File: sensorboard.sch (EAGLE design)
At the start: 18 parts, among them U1 LM1117MP-3.3, U2 LM324D

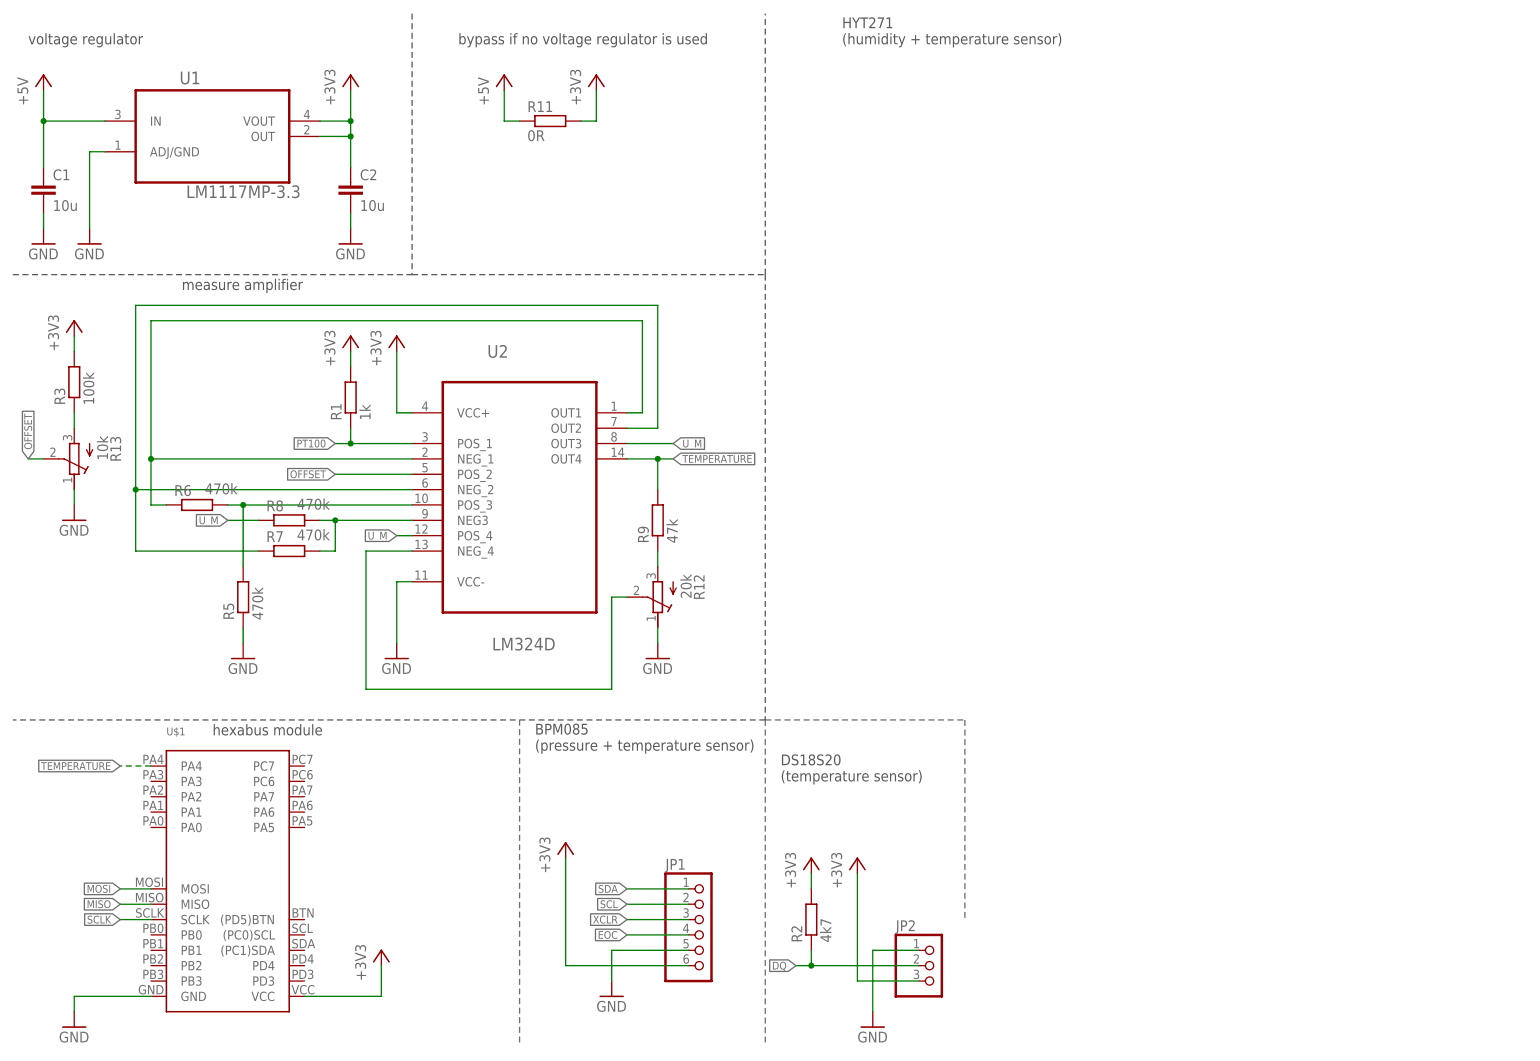
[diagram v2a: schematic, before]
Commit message: added HYT271
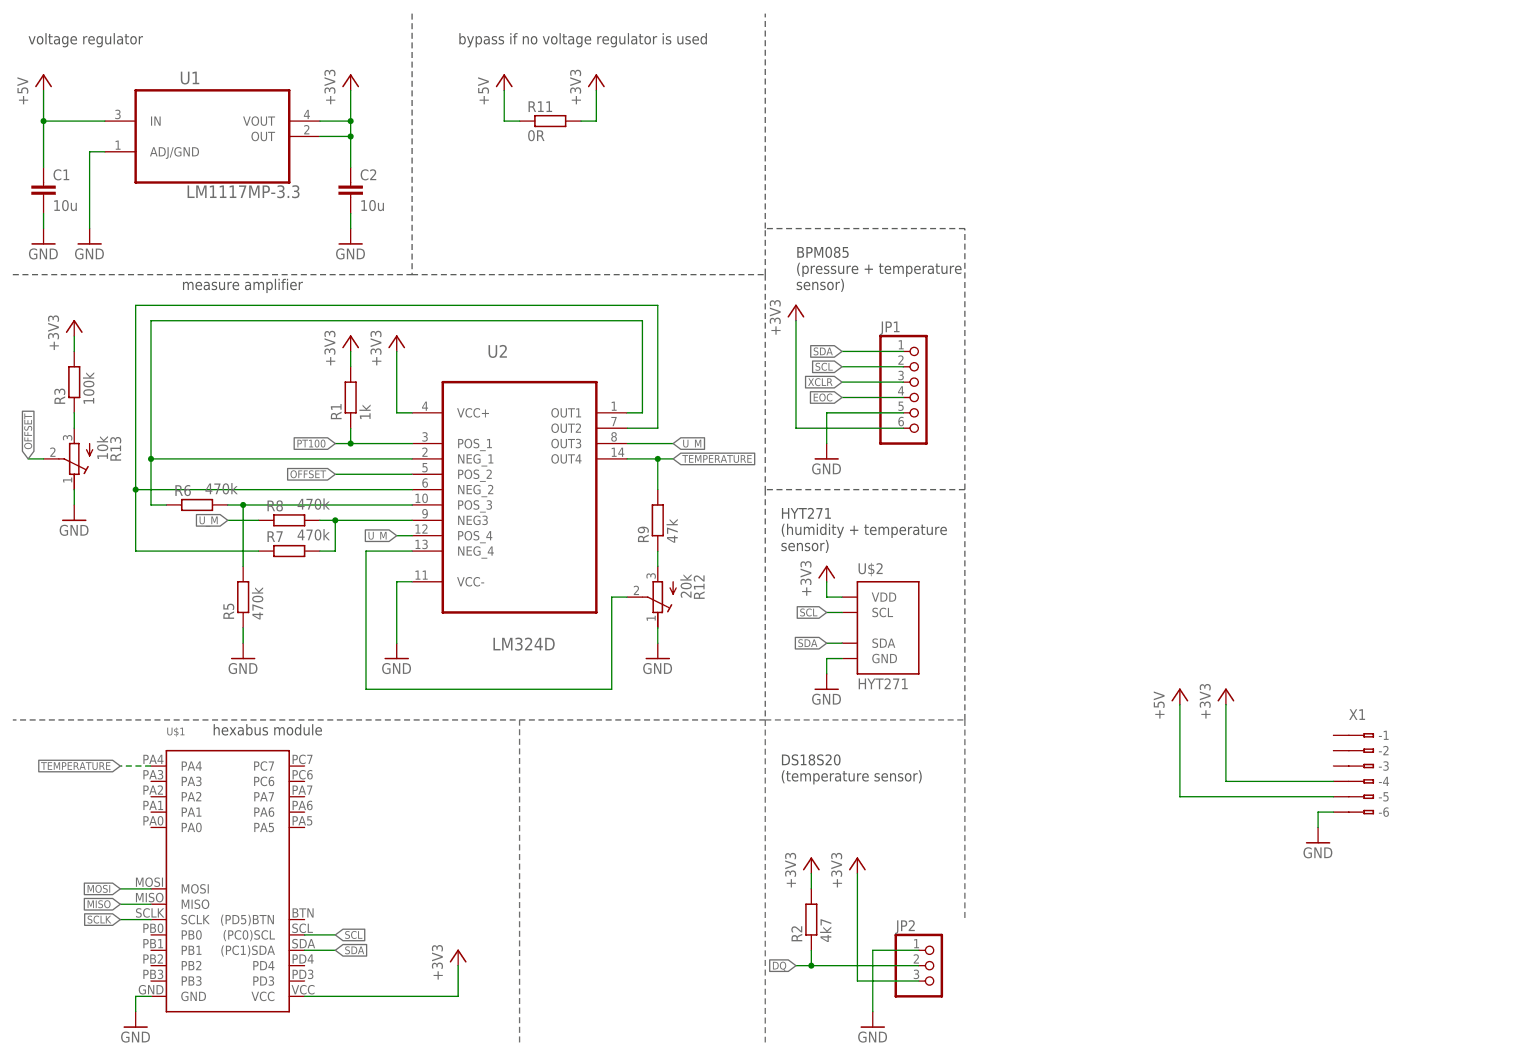
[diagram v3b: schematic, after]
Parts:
- added U$2: HYT271, humidity:HYT271
- added X1: (no value), con-wago:233-206
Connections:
- net +3V3: now also U$2.VDD, X1.B-4
- net +5V: now also X1.B-5
- net GND: now also U$2.GND, X1.B-6
- net SCL: now also U$1.(PC0)SCL, U$2.SCL
- net SDA: now also U$1.(PC1)SDA, U$2.SDA
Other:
- moved on the sheet: JP1

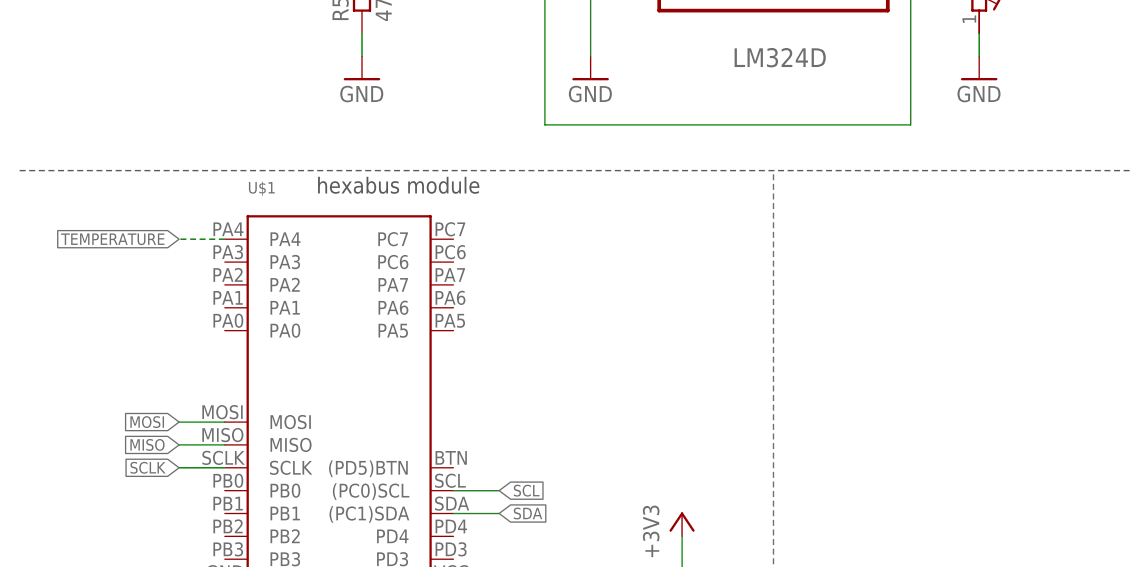
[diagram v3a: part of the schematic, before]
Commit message: connector for SPI, I2C and onewire
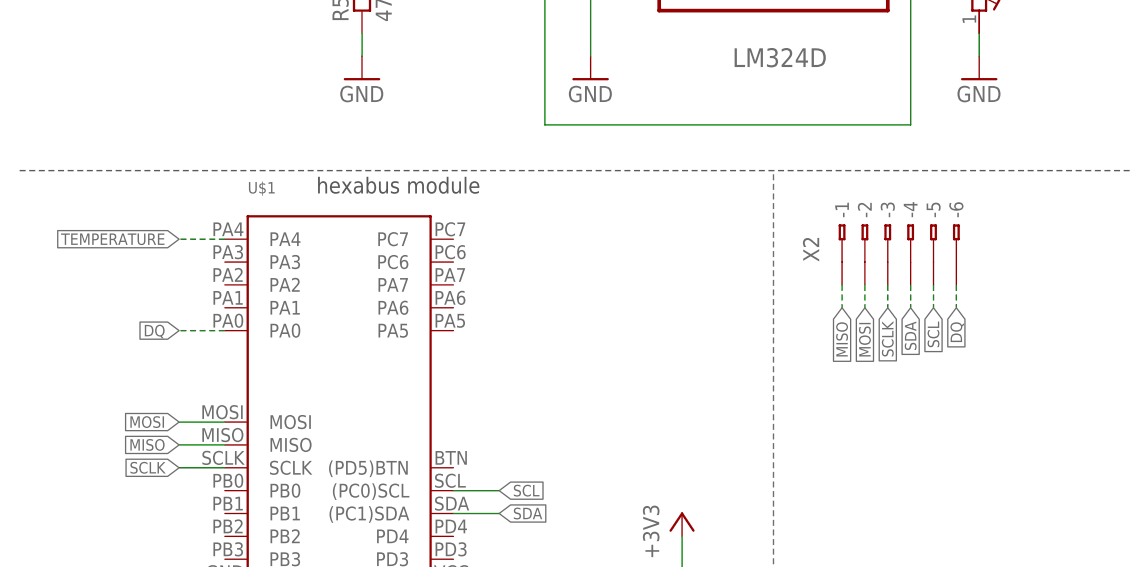
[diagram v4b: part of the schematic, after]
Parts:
- added X2: (no value), con-wago:233-206
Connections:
- net DQ: now also U$1.PA0, X2.B-6
- net MISO: now also X2.B-1
- net MOSI: now also X2.B-2
- net SCL: now also X2.B-5
- net SCLK: now also X2.B-3
- net SDA: now also X2.B-4
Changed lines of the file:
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@@
 <part name="+3V11" library="supply1" deviceset="+3V3" device=""/>
 <part name="GND12" library="supply1" deviceset="GND" device=""/>
+<part name="X2" library="con-wago" deviceset="233-206" device=""/>
 </parts>
 <sheets>
@@
 <instance part="+3V11" gate="G$1" x="139.7" y="83.82"/>
 <instance part="GND12" gate="1" x="139.7" y="63.5"/>
+<instance part="X2" gate="G$1" x="101.6" y="53.34" rot="R90"/>
 </instances>
 <busses>
@@
 <label x="22.86" y="30.48" size="1.27" layer="95" rot="R180" xref="yes"/>
 </segment>
+<segment>
+<pinref part="X2" gate="G$1" pin="B-2"/>
+<wire x1="99.06" y1="45.72" x2="99.06" y2="43.18" width="0.1524" layer="91" style="longdash"/>
+<label x="99.06" y="43.18" size="1.27" layer="95" rot="R270" xref="yes"/>
+</segment>
 </net>
 <net name="MISO" class="0">
@@
 <label x="22.86" y="27.94" size="1.27" layer="95" rot="R180" xref="yes"/>
 </segment>
+<segment>
+<pinref part="X2" gate="G$1" pin="B-1"/>
+<wire x1="96.52" y1="45.72" x2="96.52" y2="43.18" width="0.1524" layer="91" style="longdash"/>
+<label x="96.52" y="43.18" size="1.27" layer="95" rot="R270" xref="yes"/>
+</segment>
 </net>
 <net name="SCLK" class="0">
@@
 <label x="22.86" y="25.4" size="1.27" layer="95" rot="R180" xref="yes"/>
 </segment>
+<segment>
+<pinref part="X2" gate="G$1" pin="B-3"/>
+<wire x1="101.6" y1="45.72" x2="101.6" y2="43.18" width="0.1524" layer="91" style="longdash"/>
+<label x="101.6" y="43.18" size="1.27" layer="95" rot="R270" xref="yes"/>
+</segment>
 </net>
 <net name="SDA" class="0">
@@
 <label x="58.42" y="20.32" size="1.27" layer="95" xref="yes"/>
 </segment>
+<segment>
+<pinref part="X2" gate="G$1" pin="B-4"/>
+<wire x1="104.14" y1="45.72" x2="104.14" y2="43.18" width="0.1524" layer="91" style="longdash"/>
+<label x="104.14" y="43.18" size="1.27" layer="95" rot="R270" xref="yes"/>
+</segment>
 </net>
 <net name="SCL" class="0">
@@
 <wire x1="53.34" y1="22.86" x2="58.42" y2="22.86" width="0.1524" layer="91"/>
 <label x="58.42" y="22.86" size="1.27" layer="95" xref="yes"/>
+</segment>
+<segment>
+<pinref part="X2" gate="G$1" pin="B-5"/>
+<wire x1="106.68" y1="45.72" x2="106.68" y2="43.18" width="0.1524" layer="91" style="longdash"/>
+<label x="106.68" y="43.18" size="1.27" layer="95" rot="R270" xref="yes"/>
 </segment>
 </net>
@@
 <label x="134.62" y="17.78" size="1.27" layer="95" rot="R180" xref="yes"/>
 </segment>
-</net>
+<segment>
+<pinref part="U$1" gate="G$1" pin="PA0"/>
+<wire x1="27.94" y1="40.64" x2="22.86" y2="40.64" width="0.1524" layer="91" style="longdash"/>
+<label x="22.86" y="40.64" size="1.27" layer="95" rot="R180" xref="yes"/>
+</segment>
+<segment>
+<pinref part="X2" gate="G$1" pin="B-6"/>
+<wire x1="109.22" y1="45.72" x2="109.22" y2="43.18" width="0.1524" layer="91" style="longdash"/>
+<label x="109.22" y="43.18" size="1.27" layer="95" rot="R270" xref="yes"/>
+</segment>
+</net>

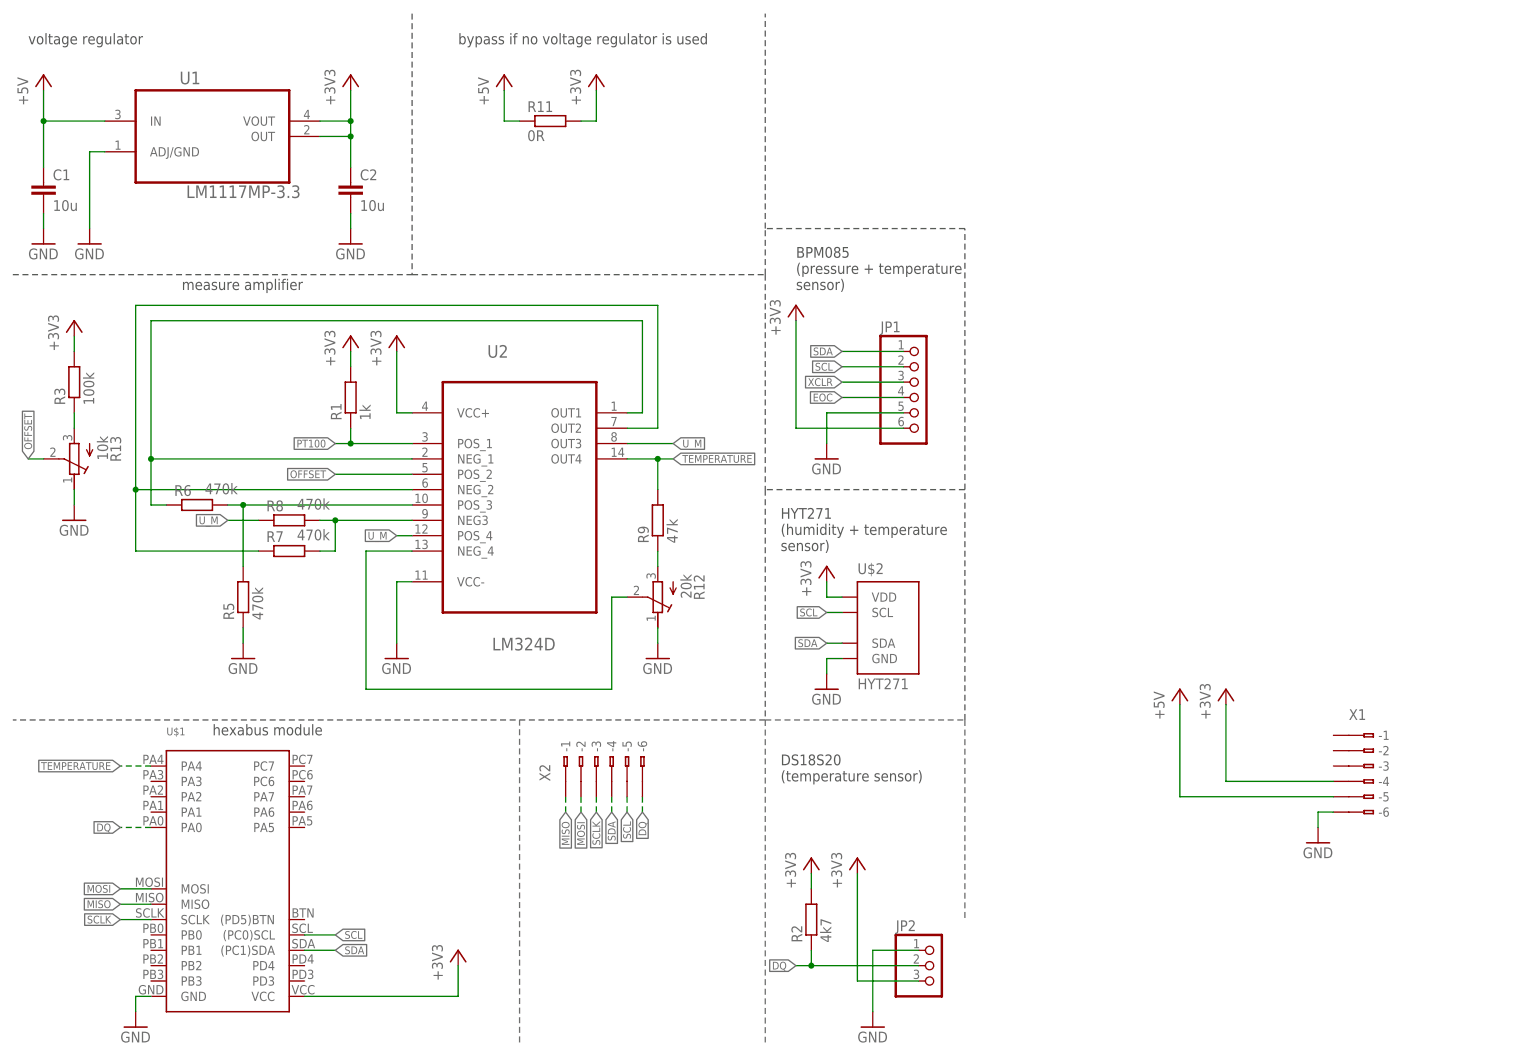
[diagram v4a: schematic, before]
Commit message: added GPIO safety cicuits
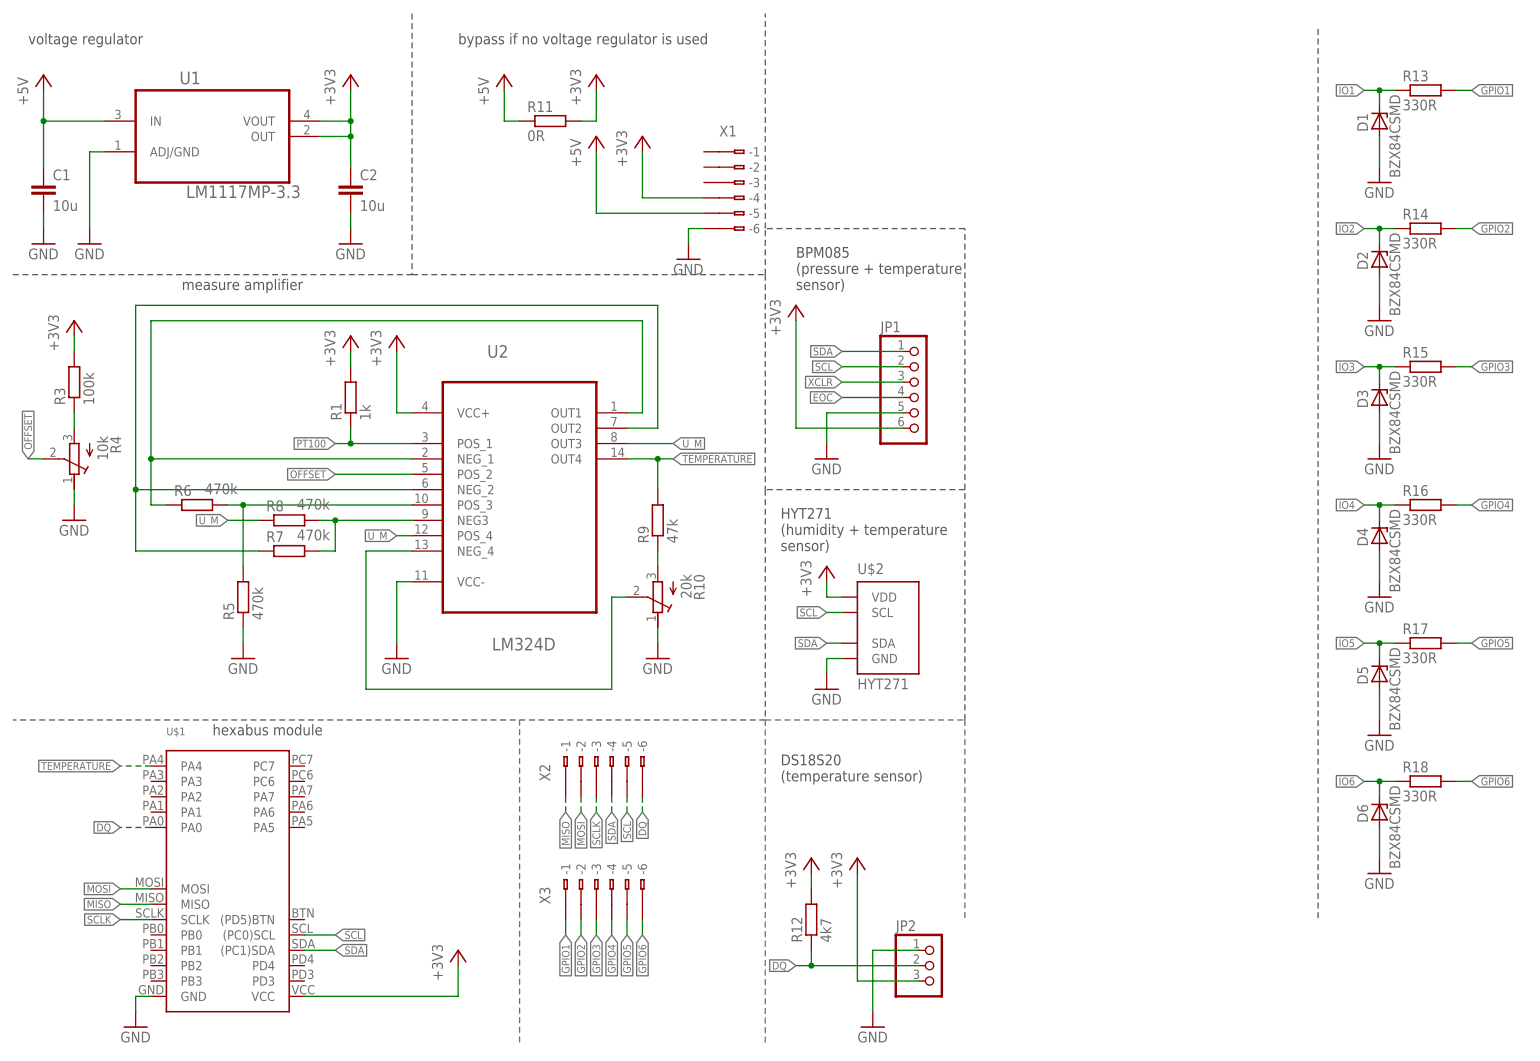
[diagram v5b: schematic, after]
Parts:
- removed R2: 4k7, rcl:R-EU_R0805
- added D1, D2, D3, D4, D5, D6: BZX84CSMD, diode:BZX84CSMD
- added R10: 20k, rcl:R-TRIMMT93YB
- added R14, R15, R16, R17, R18: 330R, rcl:R-EU_R0805
- added R4: 10k, rcl:R-TRIMMT93YB
- added X3: (no value), con-wago:233-206
- R12: value 20k -> 4k7; device rcl:R-TRIMMT93YB -> rcl:R-EU_R0805
- R13: value 10k -> 330R; device rcl:R-TRIMMT93YB -> rcl:R-EU_R0805
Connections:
- new net GPIO1: R13.2, X3.B-1
- new net GPIO2: R14.2, X3.B-2
- new net GPIO3: R15.2, X3.B-3
- new net GPIO4: R16.2, X3.B-4
- new net GPIO5: R17.2, X3.B-5
- new net GPIO6: R18.2, X3.B-6
- new net IO1: D1.C, R13.1
- new net IO2: D2.C, R14.1
- new net IO3: D3.C, R15.1
- new net IO4: D4.C, R16.1
- new net IO5: D5.C, R17.1
- new net IO6: D6.C, R18.1
- net +3V3: now also R12.2; no longer R2.2
- net DQ: now also R12.1; no longer R2.1
- net GND: now also D1.A, D2.A, D3.A, D4.A, D5.A, D6.A, R10.E, R4.E; no longer R12.E, R13.E
- net N$5: now also R10.S; no longer R12.S
- net N$6: now also R10.A; no longer R12.A
- net N$7: now also R4.A; no longer R13.A
- net OFFSET: now also R4.S; no longer R13.S
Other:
- moved on the sheet: X1
